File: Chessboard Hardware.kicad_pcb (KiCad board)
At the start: 2 copper layers, 200 x 200 mm, 100 parts, among them J1 Conn_01x04_Pin

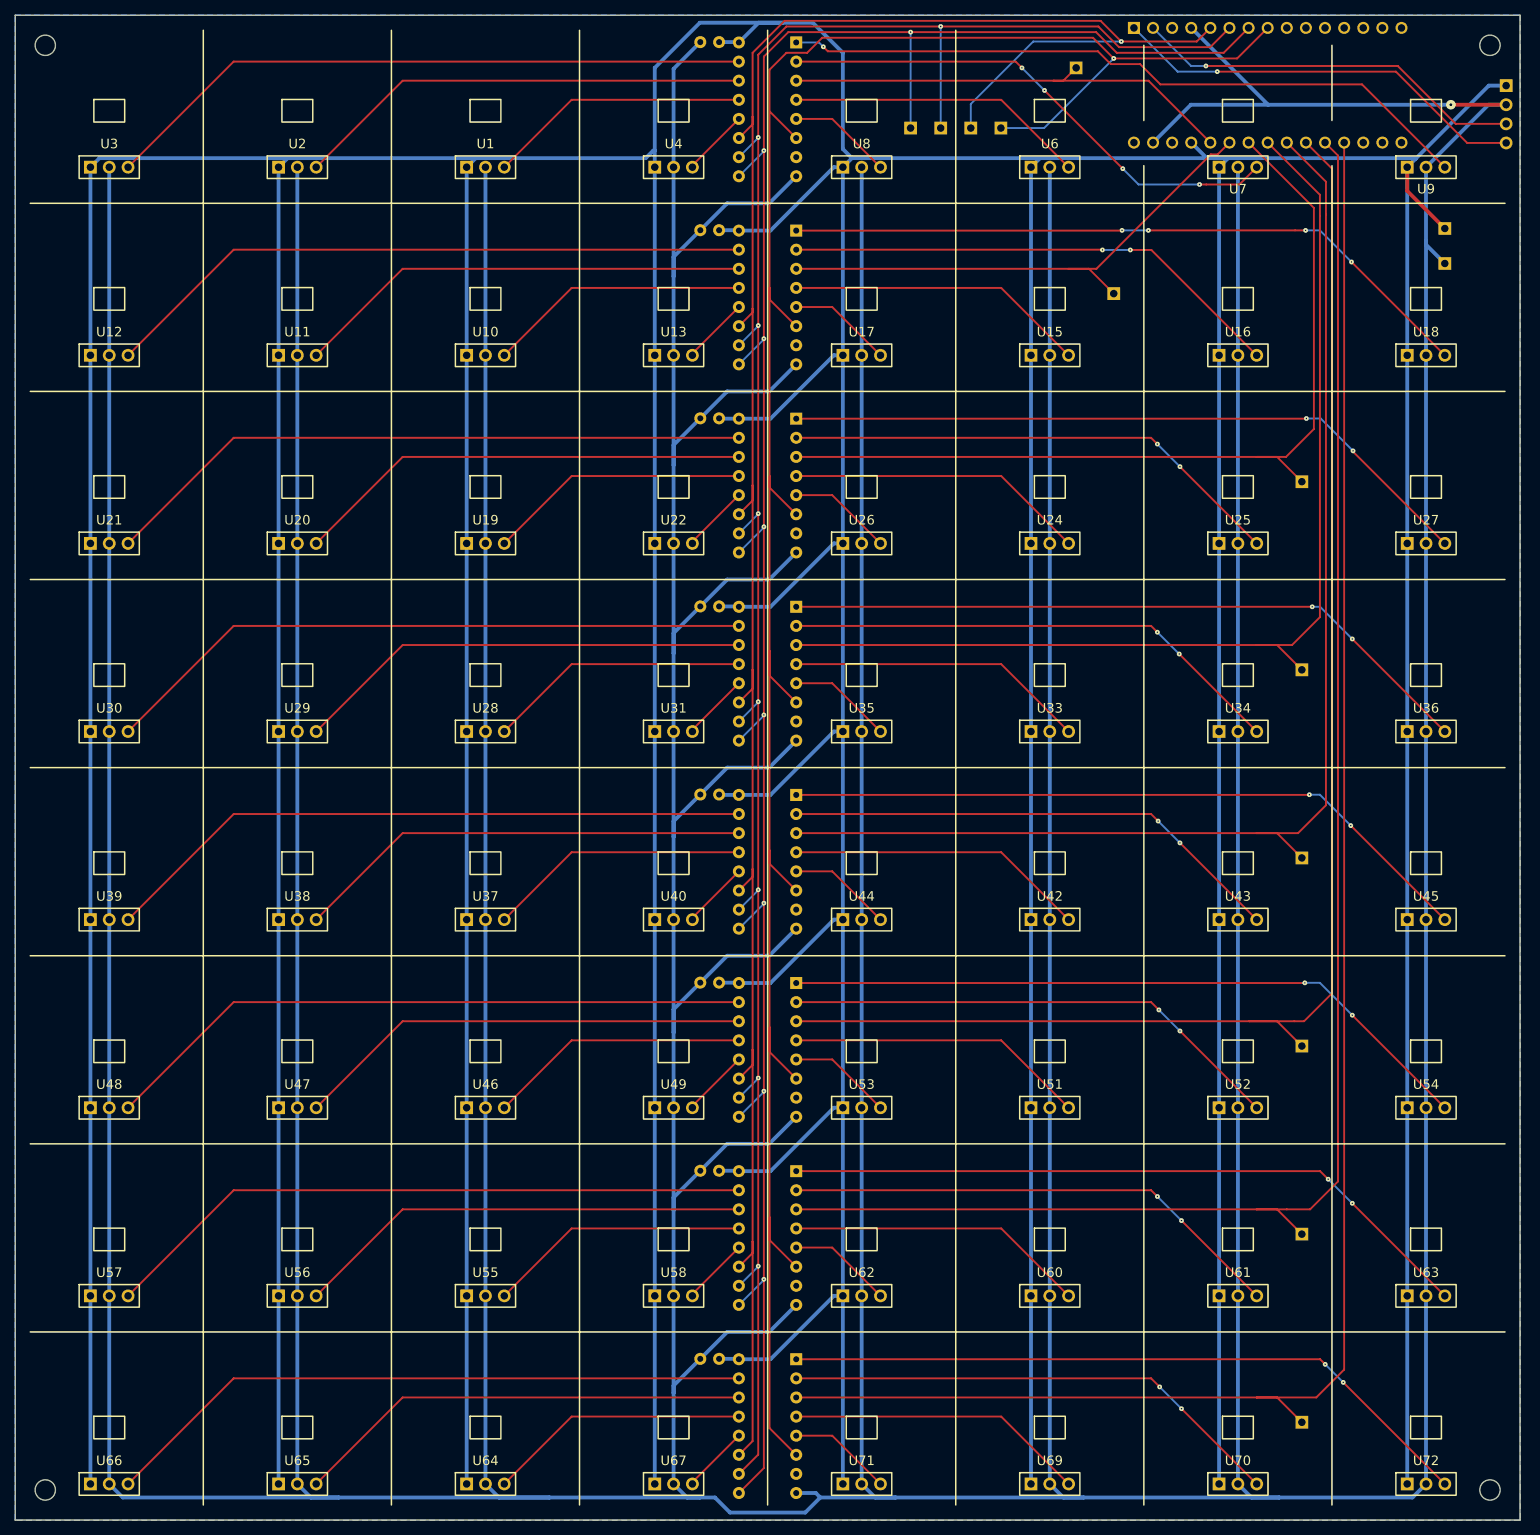
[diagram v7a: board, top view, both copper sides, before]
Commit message: Done with silkscreens
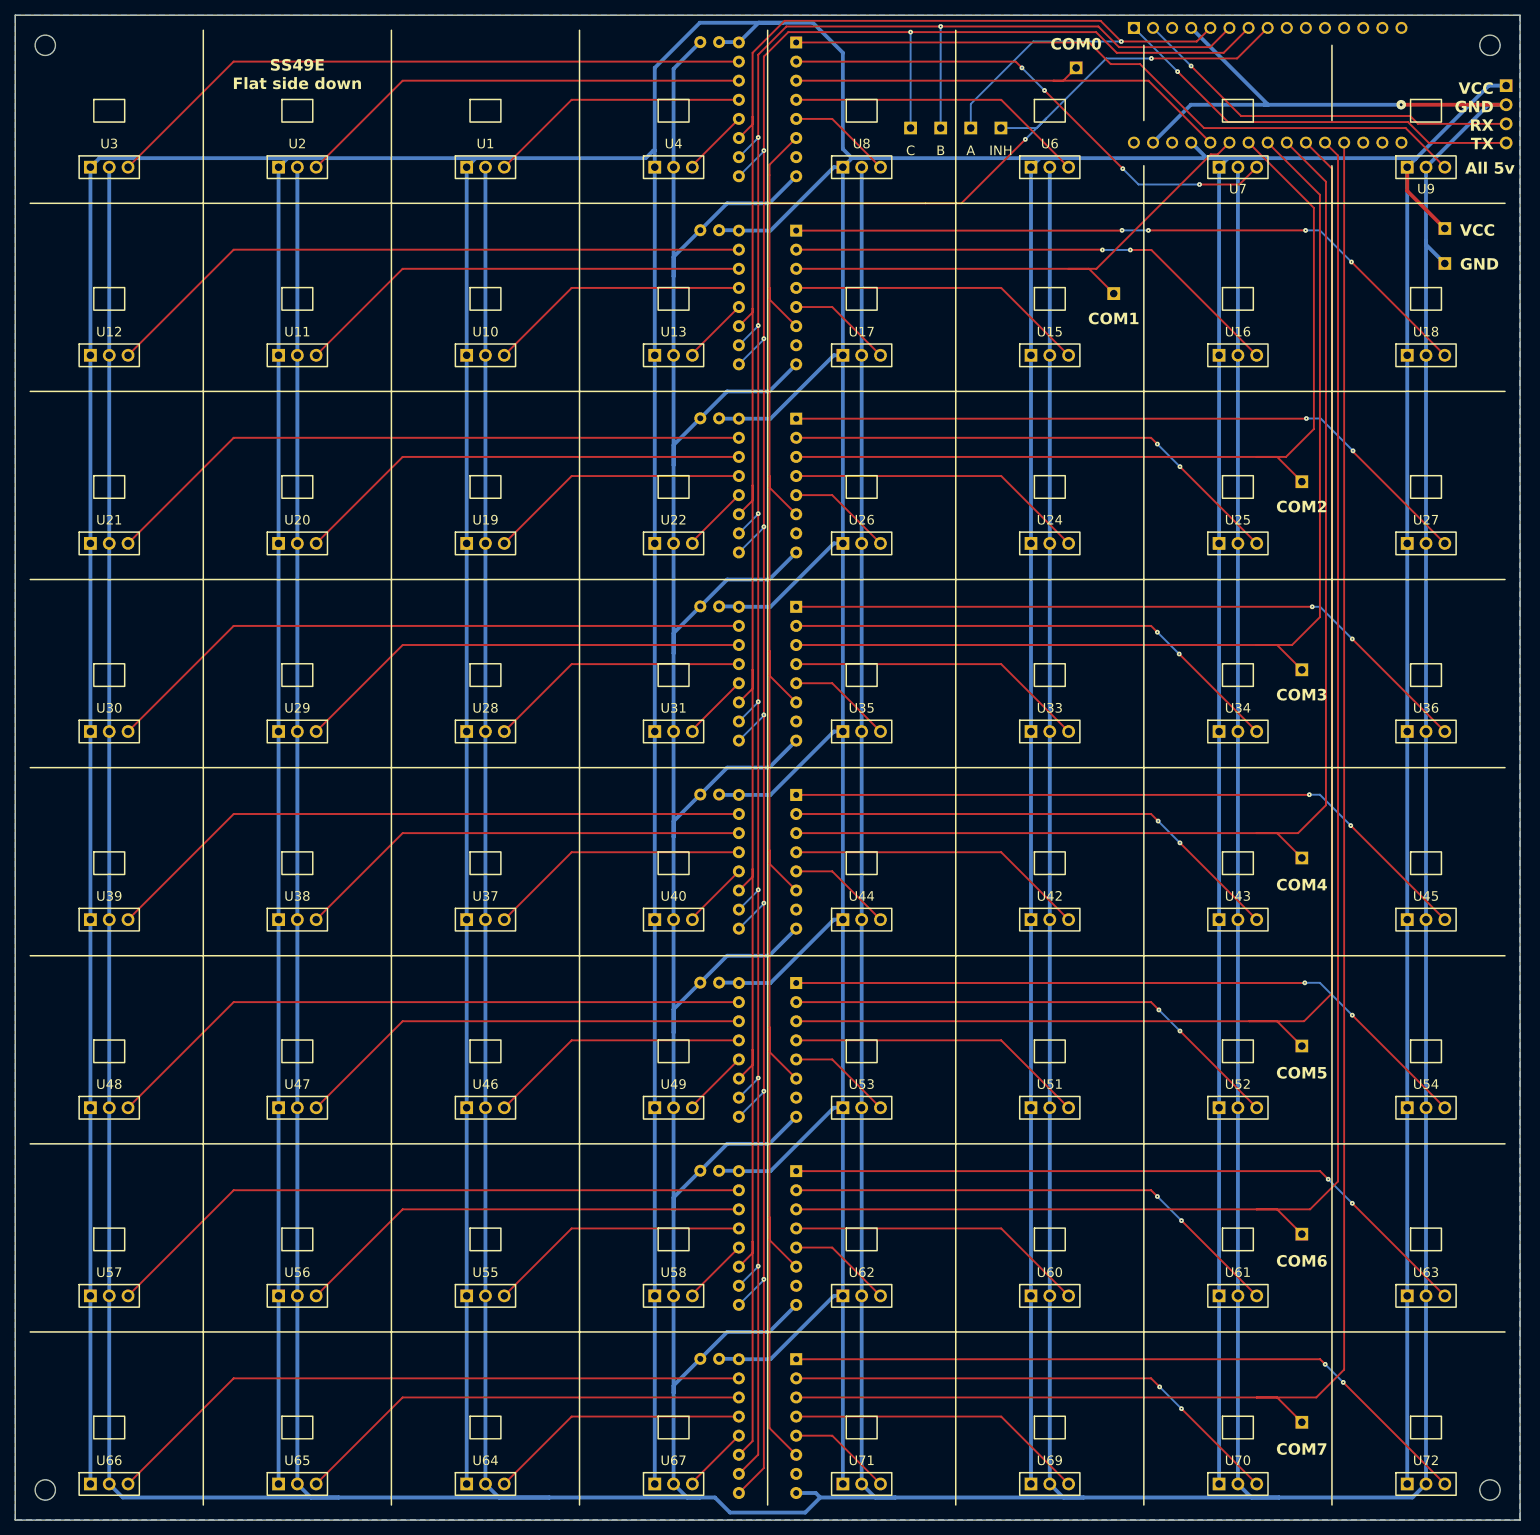
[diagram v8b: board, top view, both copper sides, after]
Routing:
- net /INH: track 324.7 -> 304.8 mm, vias 1 -> 2
- net GND: track 1878.6 -> 1879.2 mm
- net Net-(U5-Y4): vias 1 -> 0
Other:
- board text added: "100nF"
- board text added: "A"
- board text added: "All 5v"
- board text added: "Arduino Nano"
- board text added: "B"
- board text added: "C"
- board text added: "COM0"
- board text added: "COM1"
- board text added: "COM2"
- board text added: "COM3"
- board text added: "COM4"
- board text added: "COM5"
- board text added: "COM6"
- board text added: "COM7"
- board text added: "GND"
- board text added: "INH"
- board text added: "SN74HC4851N"
- board text added: "SS49E Flat side down"
- board text added: "VCC"
- board text added: "VCC GND RX TX"
